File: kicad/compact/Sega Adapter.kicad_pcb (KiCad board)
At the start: 2 copper layers, 36.2 x 33 mm, 5 parts, among them U1 PIC16F1847

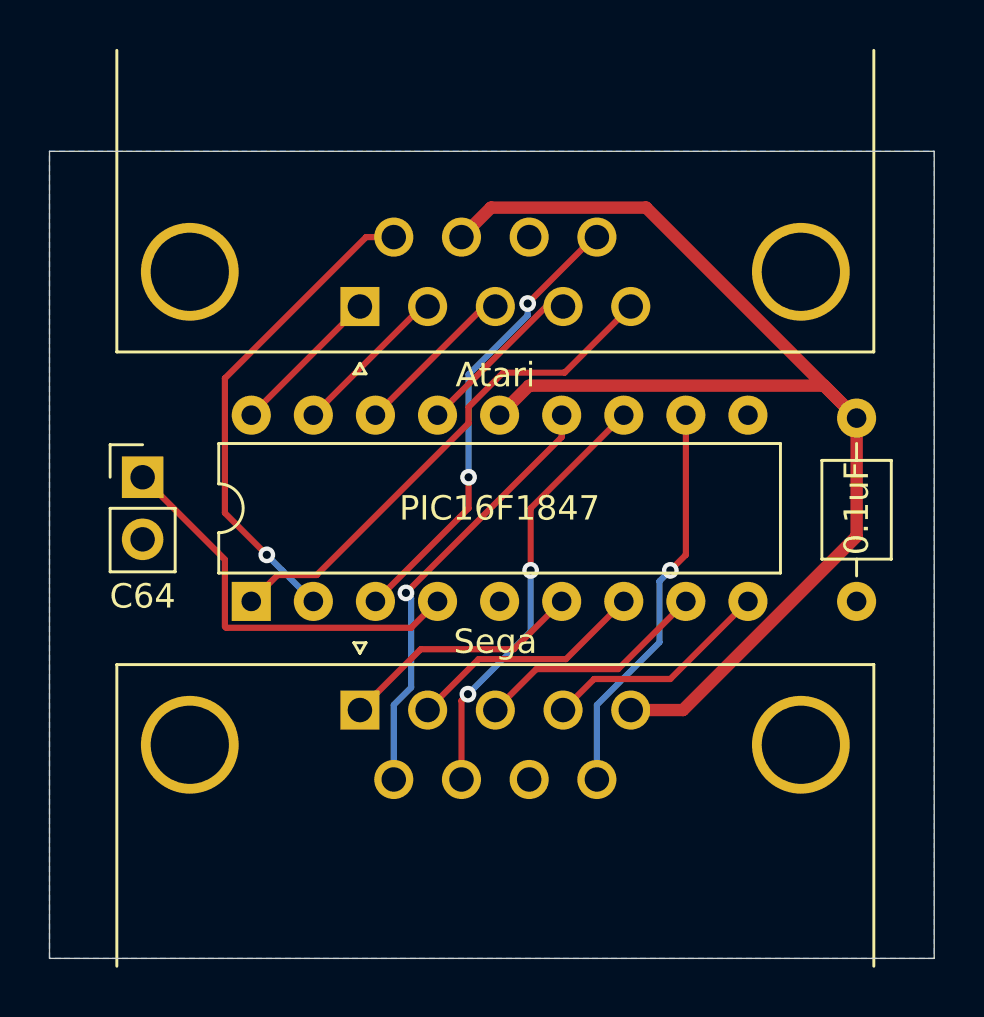
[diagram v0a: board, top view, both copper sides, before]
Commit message: Get rid of vias
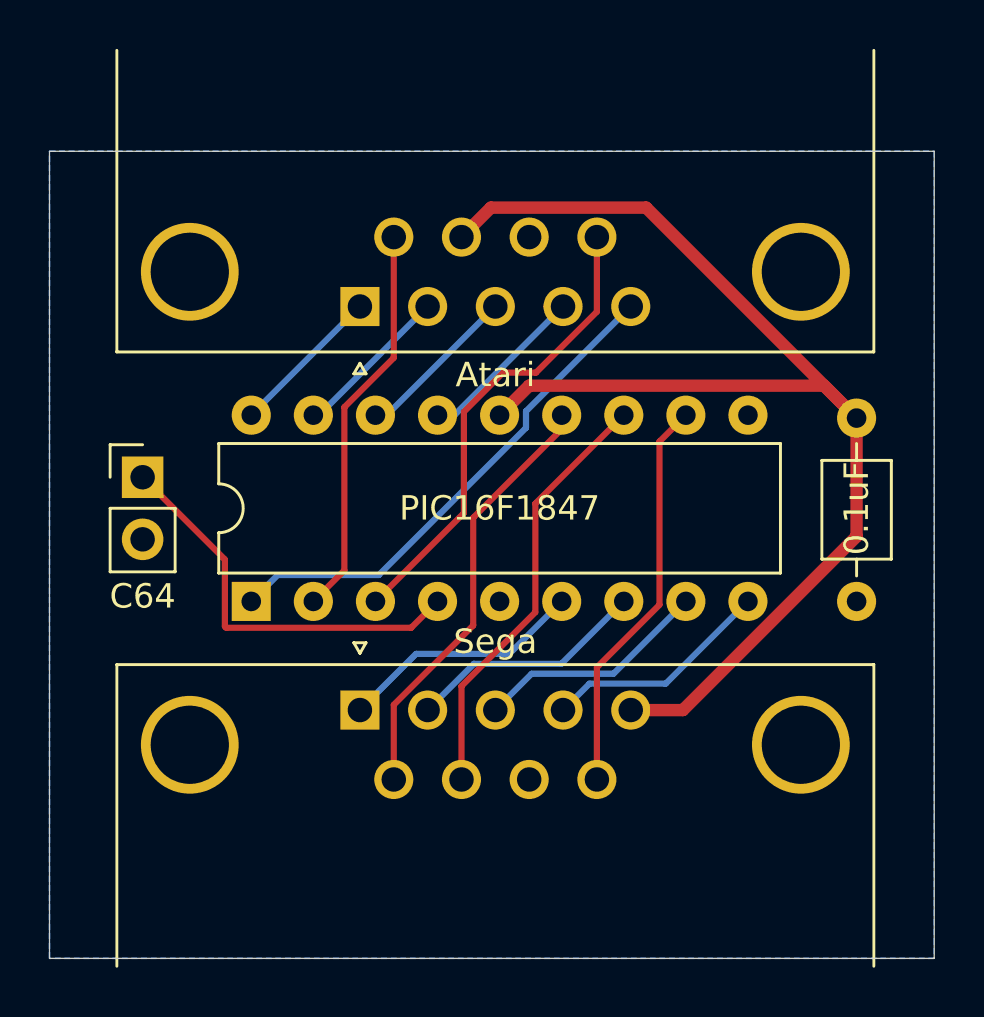
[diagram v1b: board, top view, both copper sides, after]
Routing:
- net Net-(J2-Pad6): track 19.9 -> 16.3 mm, vias 1 -> 0
- net Net-(J2-Pad9): track 18.7 -> 19.4 mm, vias 2 -> 0
- net Net-(J2-Pad4): track 6.98 -> 7.67 mm
- net Net-(J1-Pad6): track 17.9 -> 17.8 mm, vias 1 -> 0
- net Net-(J1-Pad9): vias 1 -> 0
- net Net-(J1-Pad7): vias 2 -> 0

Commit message: Switch compact adapter to IDC connector
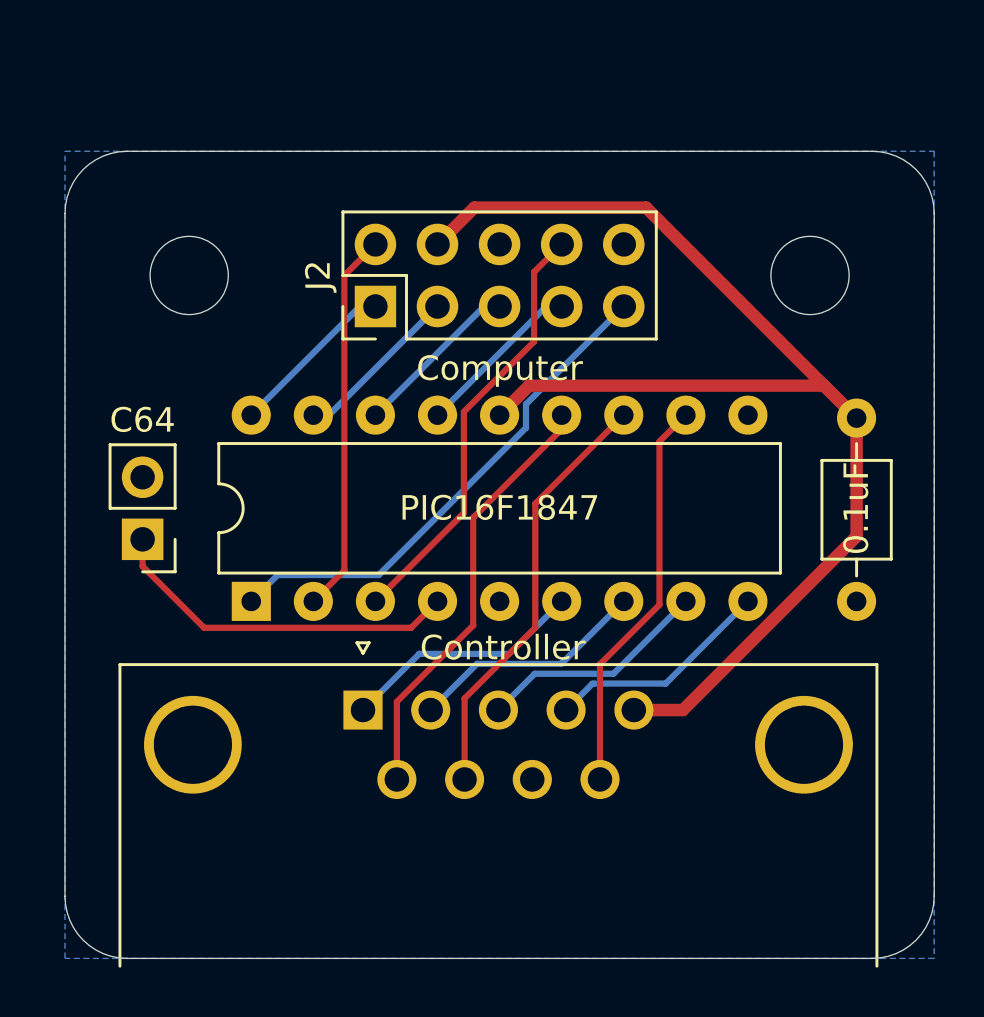
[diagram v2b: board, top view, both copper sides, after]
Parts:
- removed Atari: Atari, Connector_Dsub:DSUB-9_Female_Horizontal_P2.77x2.84mm_EdgePinOffset7.70mm_Housed_MountingHolesOffset9.12mm
- added J2: Computer, Connector_PinHeader_2.54mm:PinHeader_2x05_P2.54mm_Vertical, F.Cu at (141.6, 119.4)
- added REF**: MountingHole_3.2mm_M3, MountingHole:MountingHole_3.2mm_M3, F.Cu at (159.4, 118.1)
- added REF**: MountingHole_3.2mm_M3, MountingHole:MountingHole_3.2mm_M3, F.Cu at (134.0, 118.1)
- J1: renamed from Sega; value Sega -> Controller
- moved JP1 2.54 mm to (132.1, 128.9), turned to 180 degrees
- moved J1 0.13 mm to (141.1, 135.9)
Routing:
- net Net-(JP1-Pad1): track 16.7 -> 14.7 mm
- net Net-(J2-Pad8): track 19.4 -> 17.8 mm
- net Net-(J2-Pad3): track 6.75 -> 8.02 mm
- net +5V: track 52.9 -> 53.9 mm
- net Net-(J2-Pad5): track 7.21 -> 7.84 mm
- net Net-(J2-Pad1): track 6.29 -> 6.92 mm
- net Net-(J2-Pad7): track 7.67 -> 8.30 mm
- net Net-(J2-Pad2): track 16.3 -> 15.7 mm
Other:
- board size 36.2 x 33 mm -> 35.6 x 33 mm
- board text added: "Sega Controller Adapter Copyright © 2021 Eyvind Bernhardsen"
